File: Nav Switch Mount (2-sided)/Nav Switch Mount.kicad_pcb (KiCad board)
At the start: 2 copper layers, 22.3 x 12.6 mm, 9 parts, among them J1 Conn_01x06, U1 SKQUAAA010

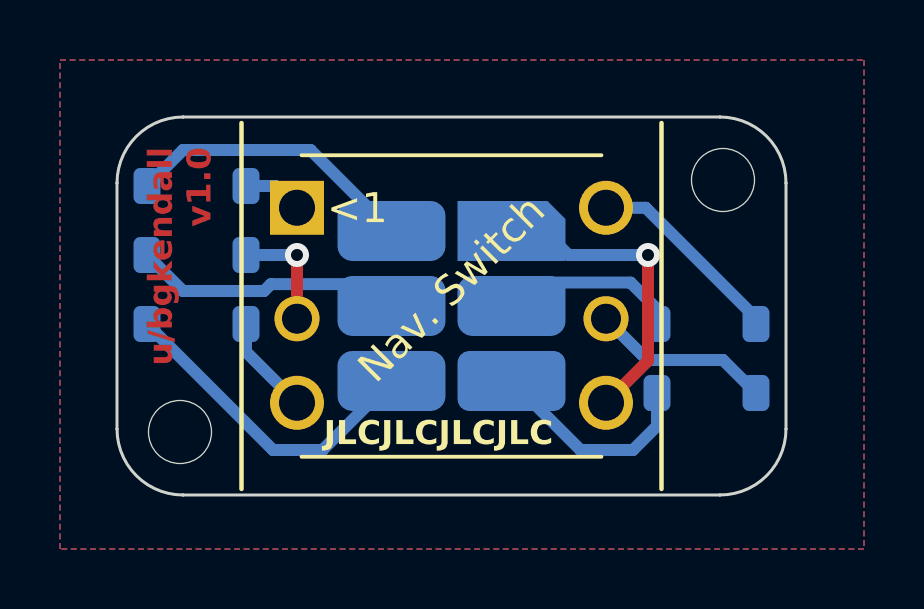
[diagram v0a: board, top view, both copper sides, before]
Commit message: Updates after producing PCB
 * Increased pad around nav. switch pins
 * Decreased size of matrix connection pads
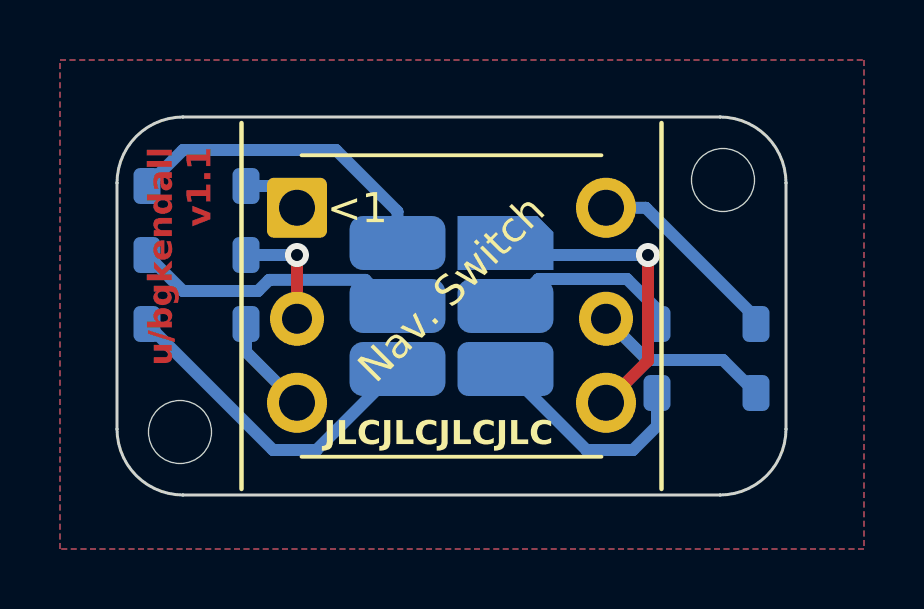
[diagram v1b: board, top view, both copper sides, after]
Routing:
- net Net-(J1-Pin_6): track 8.93 -> 10.4 mm
- net Net-(D5-A): track 4.94 -> 6.14 mm
- net Net-(D2-A): track 8.01 -> 9.16 mm
- net Net-(D1-A): track 9.77 -> 10.7 mm
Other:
- board text added: "u/bgkendall v1.1"
- board text removed: "u/bgkendall v1.0"
